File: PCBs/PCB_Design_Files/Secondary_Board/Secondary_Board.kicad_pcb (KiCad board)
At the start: 4 copper layers, 40.3 x 57.1 mm, 42 parts, among them IC1 TLV2333IDGKR, J1 Conn_FFC_8pin, J2 Conn_01x08_Pin, Q1 DMMT3904W-7-F, Q2 DMMT3904W-7-F, Q3 MMBT3904, Q4 MMBT3904, U1 DMMT5401-7-F, U2 DMMT5401-7-F, U3 DMMT5401-7-F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

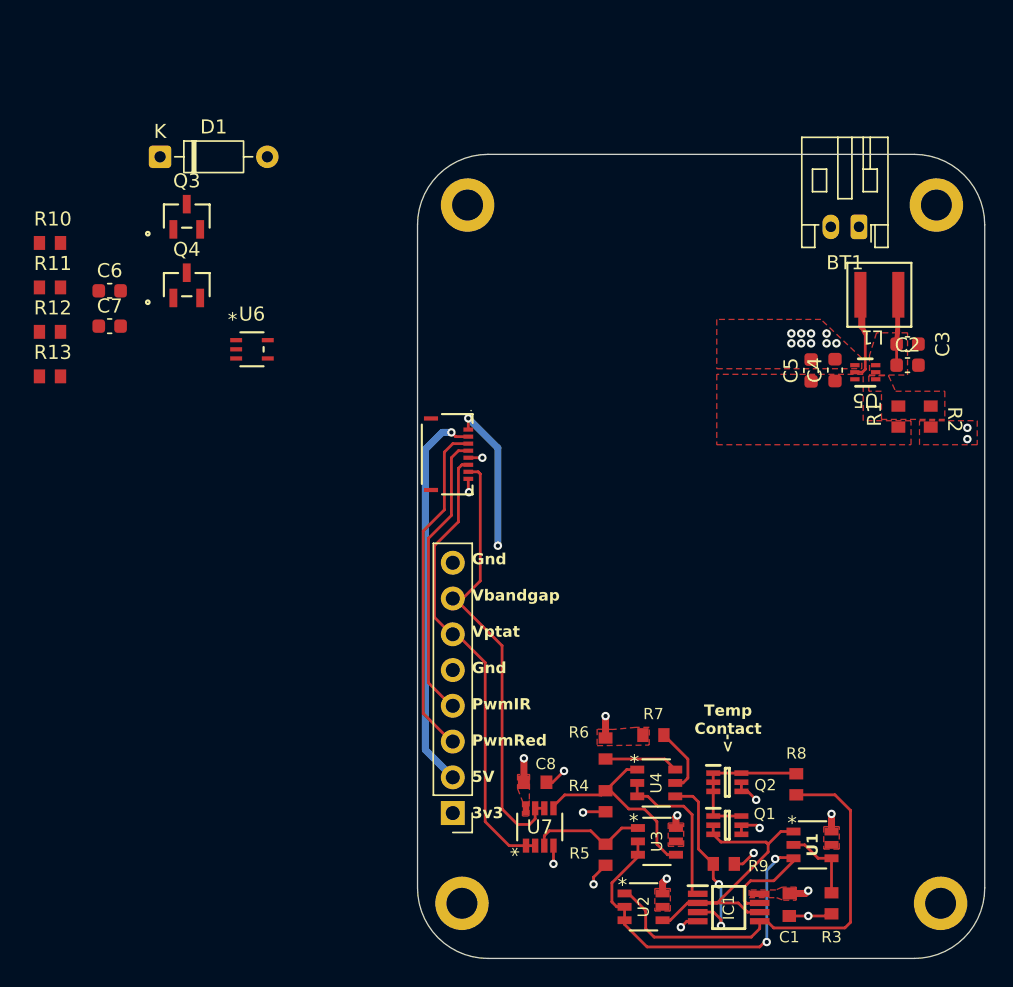
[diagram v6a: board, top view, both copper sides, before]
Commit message: boost and ldo to pcb
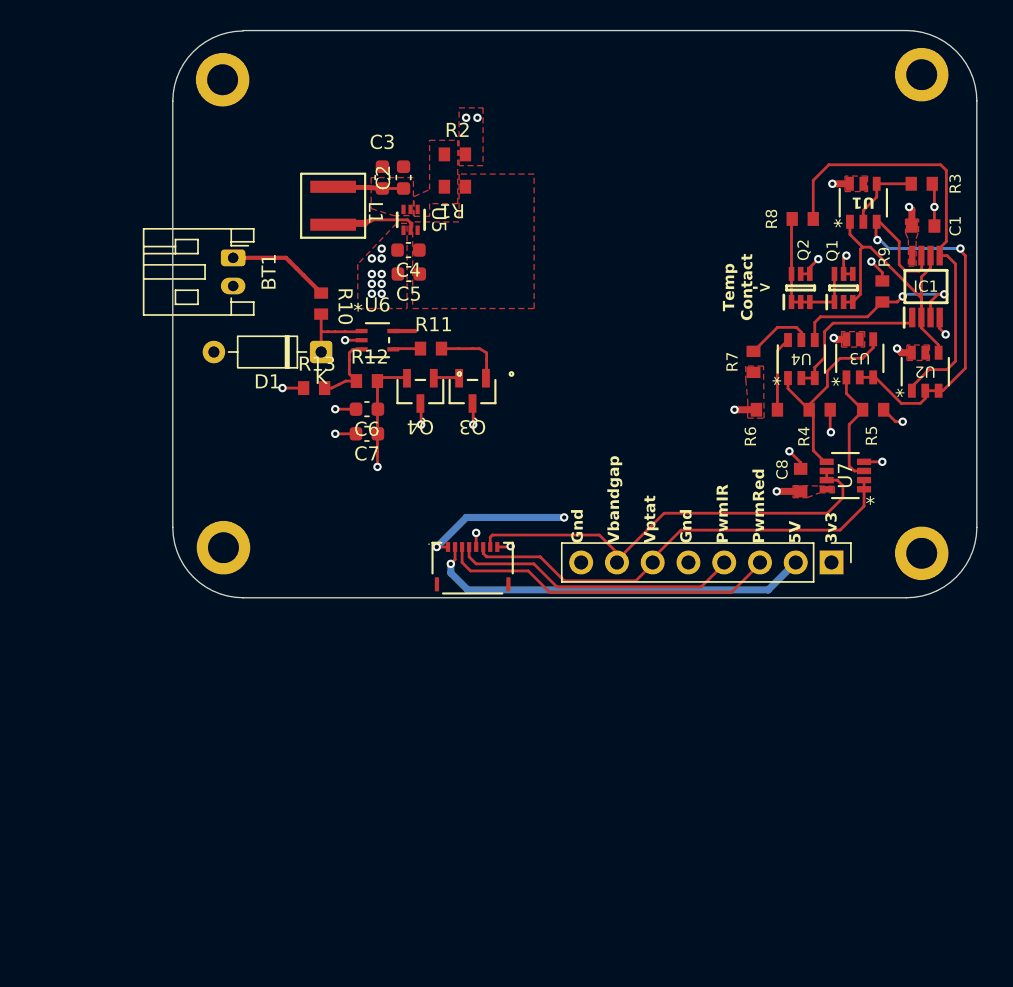
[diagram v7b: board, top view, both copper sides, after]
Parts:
- moved H3 58.9 mm to (143.7, 61.1), turned to 90 degrees
- moved R3 51.5 mm to (143.7, 68.9), turned to 0 degrees
- moved H1 51.5 mm to (94.0, 61.5), turned to 90 degrees
- moved C1 49.1 mm to (143.8, 71.9), turned to 180 degrees
- moved IC1 46.3 mm to (144.0, 76.2), turned to 90 degrees
- moved U1 45.8 mm to (139.5, 70.2), turned to 90 degrees
- moved BT1 44.5 mm to (94.8, 74.2), turned to -90 degrees
- moved U2 43.0 mm to (143.9, 82.2), turned to 90 degrees
- moved R9 42.2 mm to (140.9, 76.5), turned to 90 degrees
- moved H4 41.0 mm to (143.7, 95.1), turned to 90 degrees
- moved R8 40.2 mm to (135.2, 71.4), turned to 180 degrees
- moved L1 39.3 mm to (101.8, 70.5), turned to -90 degrees
- moved C3 39.1 mm to (105.3, 68.5), turned to 90 degrees
- moved Q1 39.0 mm to (138.1, 76.3), turned to 90 degrees
- moved R2 38.6 mm to (110.5, 66.8), turned to 0 degrees
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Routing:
- net GND: vias 22 -> 26
- net /Power Management/+5V: vias 0 -> 2
- net +3V3: vias 8 -> 9
- added copper zone on In2.Cu, net /Power Management/+5V
- removed copper zone on In2.Cu, net +5V
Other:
- board size 40.3 x 57.1 mm -> 57.1 x 40.3 mm

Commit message: add driver components
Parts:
- added LED1: SFH 7018A, Project Footprints:SFH_7018A_LEDs, F.Cu at (116.1, 75.2)
- added Q5: 2N7002, Project Footprints:2N7002, F.Cu at (124.1, 81.8)
- added Q6: BSS84, Project Footprints:BSS84, F.Cu at (117.6, 69.0)
- added Q7: 2N7002, Project Footprints:2N7002, F.Cu at (118.1, 82.3)
- added Q8: BSS84, Project Footprints:BSS84, F.Cu at (124.0, 69.0)
- added U8: OPA333AIDCKR, Project Footprints:OPA333, F.Cu at (124.6, 74.8)
